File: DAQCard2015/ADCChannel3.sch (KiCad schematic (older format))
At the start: 50 parts, among them U1 LTC6403, U2 AD9219, U3 LTC6403, U4 LTC6403, U5 LTC6403

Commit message: Updates to DAQ Card including FPGA card pinout and completion of ADC Stage
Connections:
- net labels added: 18ana

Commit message: Replaces single ample with 4-channel varients. Greatly reducing part count
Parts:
- removed C1, C11, C15, C16: .01uF, symbol C
- removed C10, C2, C3, C7, C9: .1uF, symbol C
- removed C12, C13, C14, C17, C18, C19, C20, C21, C22, C4, C5, C6: C, symbol C
- removed C8: 2.2uF, symbol CP
- removed R1, R13, R14, R8: Rt, symbol R
- removed R10, R15, R16, R17, R18, R2, R3, R9: Ri, symbol R
- removed R11, R12, R19, R20, R21, R22, R5, R6: Rf, symbol R
- removed R23: 2.7k, symbol R
- removed R24: 1k, symbol R
- removed R7: 10k, symbol R
- removed U1, U3, U4, U5: LTC6403, symbol LTC6403
- removed U2: AD9219, symbol AD9219
- added C32, C33, C34: C, symbol C
- added C35: .01uF, symbol C
- added C36, C37, C38, C40, C41: .1uF, symbol C
- added C39: 2.2uF, symbol CP
- added R25, R26, R27, R28: Rt, symbol R
- added R29: 2.7k, symbol R
- added R30: 1k, symbol R
- added R31: 10k, symbol R
- added RP10: R_PACK8, symbol R_PACK8
- added RP11, RP12: Rf, symbol R_PACK4
- added U8: THS4524IDBTR, symbol THS4524IDBTR
- added U9: AD9219, symbol AD9219
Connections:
- net labels added: 3V3ana, VOCM
- net labels removed: 18ana, 3V3, Vocm
- wire segments 178 -> 192
- no-connect marks 12 -> 4

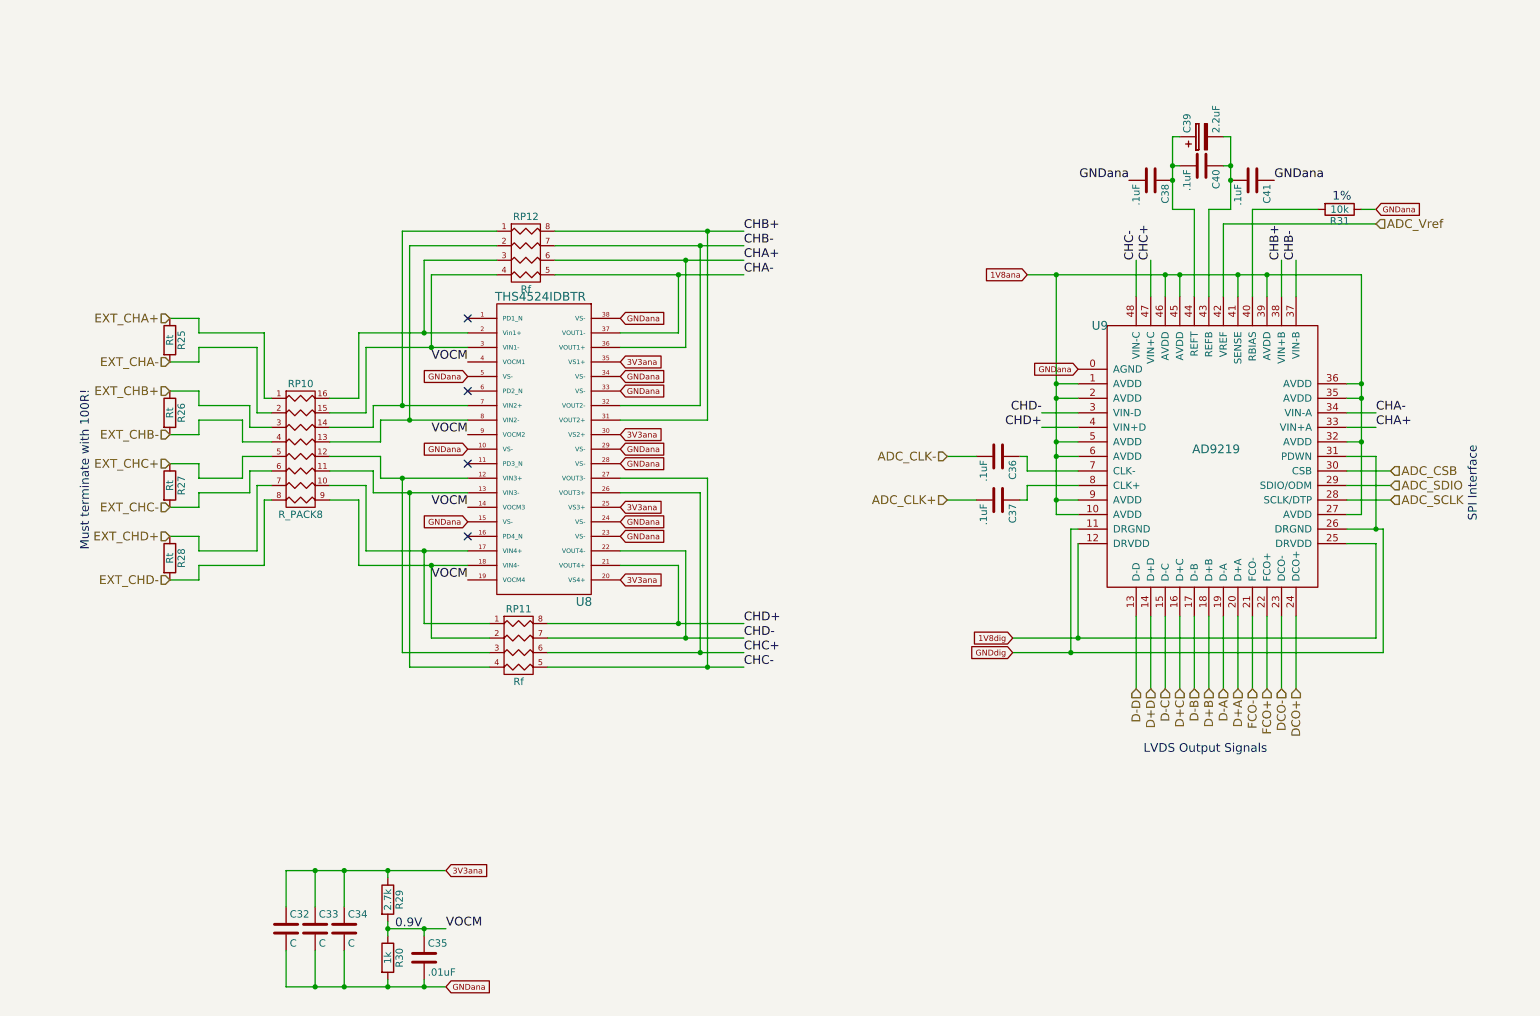
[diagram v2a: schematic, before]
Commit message: Finishes initial version of schematic(mostly). And adds a whole bunch of new footprints!
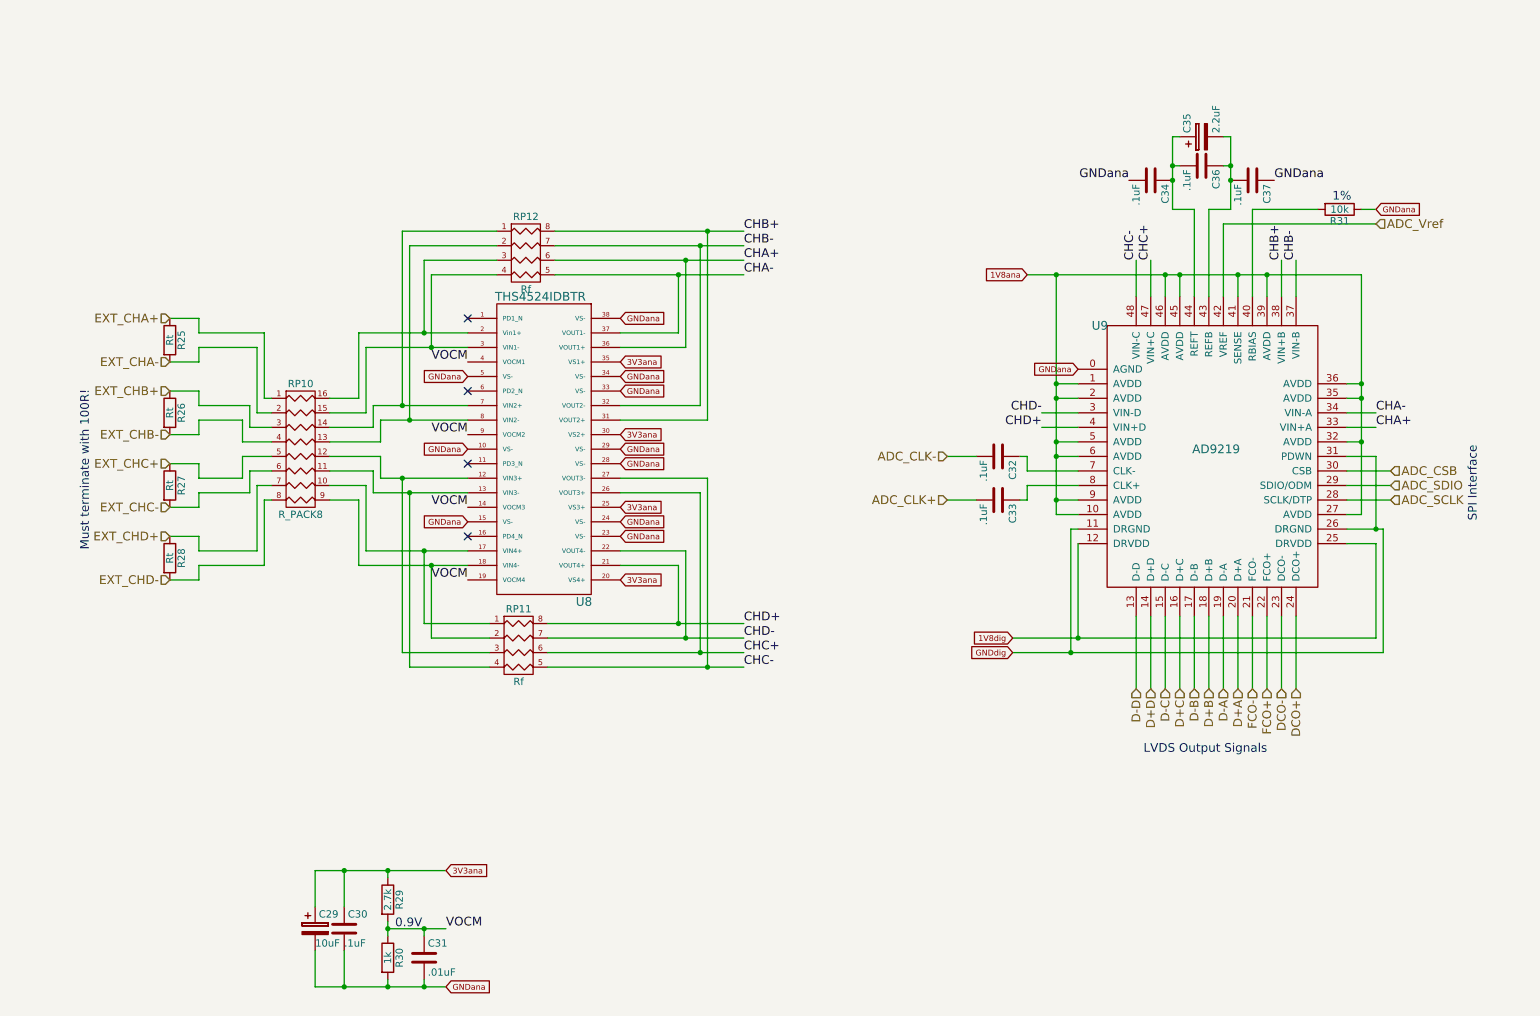
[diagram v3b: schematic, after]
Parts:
- removed C35: .01uF, symbol C
- removed C38, C40, C41: .1uF, symbol C
- removed C39: 2.2uF, symbol CP
- added C29: 10uF, extras:SMD_Cap_3mmDia, symbol CP
- added C30: .1uF, Capacitors_SMD:C_0603, symbol C
- added C31: .01uF, Capacitors_SMD:C_0603, symbol C
- added C35: 2.2uF, extras:SMD_Cap_3mmDia, symbol CP
- C32, C33, C34: value C -> .1uF; footprint (none) -> Capacitors_SMD:C_0603
- C36, C37: footprint (none) -> Capacitors_SMD:C_0603
- R25, R26, R27, R28, R29, R30, R31: footprint (none) -> Resistors_SMD:R_0603
- RP10: footprint (none) -> extras:R8_MNR18
- RP11, RP12: footprint (none) -> extras:R4-MNR04
- U8: footprint (none) -> Housings_SSOP:TSSOP-38_4.4x9.7mm_Pitch0.5mm
- U9: footprint (none) -> SMD_Packages:QFN-48-1EP
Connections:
- net 3V3ana: now also C29.1, C30.1; no longer C32.1, C33.1, C34.1
- net ADC_CLK+: now also C33.2; no longer C37.2
- net ADC_CLK-: now also C32.2; no longer C36.2
- net GNDana: now also C37.1, C29.2, C30.2, C31.2; no longer C32.2, C33.2
- net VOCM: now also C31.1
- net at U9.43 (REFB): now also C36.1, C37.2, C35.2
- net at U9.44 (REFT): now also C34.1, C36.2, C35.1
- net at U9.7 (CLK-): now also C32.1; no longer C36.1
- net at U9.8 (CLK+): now also C33.1; no longer C37.1
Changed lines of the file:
@@
 $Comp
 L AD9219 U9
-U 1 1 55CFF5AE
+U 1 1 55CFF5AD
 P 9050 3700
 F 0 "U9" H 8250 4650 60  0000 C CNN
 F 1 "AD9219" H 9050 3800 60  0000 C CNN
-F 2 "" H 8650 3700 60  0000 C CNN
+F 2 "SMD_Packages:QFN-48-1EP" H 8650 3700 60  0001 C CNN
 F 3 "" H 8650 3700 60  0000 C CNN
 	1    9050 3700
@@
 $Comp
 L R R29
-U 1 1 55CFF5F7
+U 1 1 55CB5787
 P 3350 6700
 F 0 "R29" V 3430 6700 50  0000 C CNN
 F 1 "2.7k" V 3350 6700 50  0000 C CNN
-F 2 "" V 3280 6700 30  0000 C CNN
+F 2 "Resistors_SMD:R_0603" V 3280 6700 30  0001 C CNN
 F 3 "" H 3350 6700 30  0000 C CNN
 	1    3350 6700
@@
 $Comp
 L R R30
-U 1 1 55CFF5E1
+U 1 1 55CB577A
 P 3350 7100
 F 0 "R30" V 3430 7100 50  0000 C CNN
 F 1 "1k" V 3350 7100 50  0000 C CNN
-F 2 "" V 3280 7100 30  0000 C CNN
+F 2 "Resistors_SMD:R_0603" V 3280 7100 30  0001 C CNN
 F 3 "" H 3350 7100 30  0000 C CNN
 	1    3350 7100
@@
 Must terminate with 100R!
 $Comp
-L C C32
-U 1 1 55CFF5C8
-P 2650 6900
-F 0 "C32" H 2675 7000 50  0000 L CNN
-F 1 "C" H 2675 6800 50  0000 L CNN
-F 2 "" H 2688 6750 30  0000 C CNN
-F 3 "" H 2650 6900 60  0000 C CNN
-	1    2650 6900
-	1    0    0    -1
-$EndComp
-$Comp
-L C C33
-U 1 1 55CFF5B8
-P 2850 6900
-F 0 "C33" H 2875 7000 50  0000 L CNN
-F 1 "C" H 2875 6800 50  0000 L CNN
-F 2 "" H 2888 6750 30  0000 C CNN
-F 3 "" H 2850 6900 60  0000 C CNN
-	1    2850 6900
-	1    0    0    -1
-$EndComp
-$Comp
-L C C34
-U 1 1 55CFF5BE
+L C C30
+U 1 1 55CB575B
 P 3050 6900
-F 0 "C34" H 3075 7000 50  0000 L CNN
-F 1 "C" H 3075 6800 50  0000 L CNN
-F 2 "" H 3088 6750 30  0000 C CNN
+F 0 "C30" H 3075 7000 50  0000 L CNN
+F 1 ".1uF" H 3050 6800 50  0000 L CNN
+F 2 "Capacitors_SMD:C_0603" H 3088 6750 30  0001 C CNN
 F 3 "" H 3050 6900 60  0000 C CNN
 	1    3050 6900
@@
 ADC_SCLK
 $Comp
-L C C36
-U 1 1 55CFF5C1
+L C C32
+U 1 1 55CB5767
 P 7550 3650
-F 0 "C36" H 7575 3750 50  0000 L CNN
+F 0 "C32" H 7575 3750 50  0000 L CNN
 F 1 ".1uF" H 7575 3550 50  0000 L CNN
-F 2 "" H 7588 3500 30  0000 C CNN
+F 2 "Capacitors_SMD:C_0603" H 7588 3500 30  0001 C CNN
 F 3 "" H 7550 3650 60  0000 C CNN
 	1    7550 3650
@@
 $EndComp
 $Comp
-L C C37
-U 1 1 55CFF5E3
+L C C33
+U 1 1 55CB574B
 P 7550 3950
-F 0 "C37" H 7575 4050 50  0000 L CNN
+F 0 "C33" H 7575 4050 50  0000 L CNN
 F 1 ".1uF" H 7575 3850 50  0000 L CNN
-F 2 "" H 7588 3800 30  0000 C CNN
+F 2 "Capacitors_SMD:C_0603" H 7588 3800 30  0001 C CNN
 F 3 "" H 7550 3950 60  0000 C CNN
 	1    7550 3950
@@
 DCO+
 $Comp
-L C C41
-U 1 1 55CFF5FB
+L C C37
+U 1 1 55CB5791
 P 9300 1750
-F 0 "C41" H 9325 1850 50  0000 L CNN
+F 0 "C37" H 9325 1850 50  0000 L CNN
 F 1 ".1uF" H 9325 1650 50  0000 L CNN
-F 2 "" H 9338 1600 30  0000 C CNN
+F 2 "Capacitors_SMD:C_0603" H 9338 1600 30  0001 C CNN
 F 3 "" H 9300 1750 60  0000 C CNN
 	1    9300 1750
@@
 $EndComp
 $Comp
-L C C38
-U 1 1 55CFF5D4
+L C C34
+U 1 1 55CB576A
 P 8600 1750
-F 0 "C38" H 8625 1850 50  0000 L CNN
+F 0 "C34" H 8625 1850 50  0000 L CNN
 F 1 ".1uF" H 8625 1650 50  0000 L CNN
-F 2 "" H 8638 1600 30  0000 C CNN
+F 2 "Capacitors_SMD:C_0603" H 8638 1600 30  0001 C CNN
 F 3 "" H 8600 1750 60  0000 C CNN
 	1    8600 1750
@@
 $EndComp
 $Comp
-L C C40
-U 1 1 55CFF5D8
+L C C36
+U 1 1 55CFF5D5
 P 8950 1650
-F 0 "C40" H 8975 1750 50  0000 L CNN
+F 0 "C36" H 8975 1750 50  0000 L CNN
 F 1 ".1uF" H 8975 1550 50  0000 L CNN
-F 2 "" H 8988 1500 30  0000 C CNN
+F 2 "Capacitors_SMD:C_0603" H 8988 1500 30  0001 C CNN
 F 3 "" H 8950 1650 60  0000 C CNN
 	1    8950 1650
@@
 GNDana
 $Comp
-L CP C39
-U 1 1 55CFF605
+L CP C35
+U 1 1 55CB5797
 P 8950 1450
-F 0 "C39" H 8975 1550 50  0000 L CNN
+F 0 "C35" H 8975 1550 50  0000 L CNN
 F 1 "2.2uF" H 8975 1350 50  0000 L CNN
-F 2 "" H 8988 1300 30  0000 C CNN
+F 2 "extras:SMD_Cap_3mmDia" H 8988 1300 30  0001 C CNN
 F 3 "" H 8950 1450 60  0000 C CNN
 	1    8950 1450
@@
 $Comp
 L R R31
-U 1 1 55CFF5EE
+U 1 1 55CB5783
 P 9900 1950
 F 0 "R31" V 9980 1950 50  0000 C CNN
 F 1 "10k" V 9900 1950 50  0000 C CNN
-F 2 "" V 9830 1950 30  0000 C CNN
+F 2 "Resistors_SMD:R_0603" V 9830 1950 30  0001 C CNN
 F 3 "" H 9900 1950 30  0000 C CNN
 	1    9900 1950
@@
 $Comp
 L THS4524IDBTR U8
-U 1 1 55CFF609
+U 1 1 55CB579A
 P 4400 3700
 F 0 "U8" H 4700 2750 60  0000 C CNN
 F 1 "THS4524IDBTR" H 4400 4850 60  0000 C CNN
-F 2 "" H 4600 3800 60  0000 C CNN
+F 2 "Housings_SSOP:TSSOP-38_4.4x9.7mm_Pitch0.5mm" H 4600 3800 60  0001 C CNN
 F 3 "" H 4600 3800 60  0000 C CNN
 	1    4400 3700
@@
 $EndComp
 $Comp
-L C C35
-U 1 1 55CFF60F
+L C C31
+U 1 1 55CB57A1
 P 3600 7100
-F 0 "C35" H 3625 7200 50  0000 L CNN
+F 0 "C31" H 3625 7200 50  0000 L CNN
 F 1 ".01uF" H 3625 7000 50  0000 L CNN
-F 2 "" H 3638 6950 30  0000 C CNN
+F 2 "Capacitors_SMD:C_0603" H 3638 6950 30  0001 C CNN
 F 3 "" H 3600 7100 60  0000 C CNN
 	1    3600 7100
@@
 Connection ~ 3600 6900
 Wire Wire Line
-	2650 6500 3750 6500
-Wire Wire Line
 	3050 6500 3050 6750
 Connection ~ 3350 6500
@@
 Connection ~ 3050 6500
 Wire Wire Line
-	2650 6500 2650 6750
-Connection ~ 2850 6500
-Wire Wire Line
-	2650 7300 3750 7300
-Wire Wire Line
 	3050 7300 3050 7050
 Wire Wire Line
 	2850 7300 2850 7050
 Connection ~ 3050 7300
-Wire Wire Line
-	2650 7300 2650 7050
-Connection ~ 2850 7300
 Wire Wire Line
 	3600 7300 3600 7250
@@
 $Comp
 L R R28
-U 1 1 55CFF615
+U 1 1 55CB57A7
 P 1850 4350
 F 0 "R28" V 1930 4350 50  0000 C CNN
 F 1 "Rt" V 1850 4350 50  0000 C CNN
-F 2 "" V 1780 4350 30  0000 C CNN
+F 2 "Resistors_SMD:R_0603" V 1780 4350 30  0001 C CNN
 F 3 "" H 1850 4350 30  0000 C CNN
 	1    1850 4350
@@
 $Comp
 L R R27
-U 1 1 55CFF61F
+U 1 1 55CB57AF
 P 1850 3850
 F 0 "R27" V 1930 3850 50  0000 C CNN
 F 1 "Rt" V 1850 3850 50  0000 C CNN
-F 2 "" V 1780 3850 30  0000 C CNN
+F 2 "Resistors_SMD:R_0603" V 1780 3850 30  0001 C CNN
 F 3 "" H 1850 3850 30  0000 C CNN
 	1    1850 3850
@@
 $Comp
 L R R26
-U 1 1 55CFF626
+U 1 1 55CB57B7
 P 1850 3350
 F 0 "R26" V 1930 3350 50  0000 C CNN
 F 1 "Rt" V 1850 3350 50  0000 C CNN
-F 2 "" V 1780 3350 30  0000 C CNN
+F 2 "Resistors_SMD:R_0603" V 1780 3350 30  0001 C CNN
 F 3 "" H 1850 3350 30  0000 C CNN
 	1    1850 3350
@@
 $Comp
 L R R25
-U 1 1 55CFF62C
+U 1 1 55CB57BF
 P 1850 2850
 F 0 "R25" V 1930 2850 50  0000 C CNN
 F 1 "Rt" V 1850 2850 50  0000 C CNN
-F 2 "" V 1780 2850 30  0000 C CNN
+F 2 "Resistors_SMD:R_0603" V 1780 2850 30  0001 C CNN
 F 3 "" H 1850 2850 30  0000 C CNN
 	1    1850 2850
@@
 $Comp
 L R_PACK4 RP11
-U 1 1 55CFF635
+U 1 1 55CB57C6
 P 4250 5150
 F 0 "RP11" H 4250 5600 50  0000 C CNN
 F 1 "Rf" H 4250 5100 50  0000 C CNN
-F 2 "" H 4250 5150 60  0000 C CNN
+F 2 "extras:R4-MNR04" H 4250 5150 60  0001 C CNN
 F 3 "" H 4250 5150 60  0000 C CNN
 	1    4250 5150
@@
 $Comp
 L R_PACK4 RP12
-U 1 1 55CFF63D
+U 1 1 55CB5752
 P 4300 2450
 F 0 "RP12" H 4300 2900 50  0000 C CNN
 F 1 "Rf" H 4300 2400 50  0000 C CNN
-F 2 "" H 4300 2450 60  0000 C CNN
+F 2 "extras:R4-MNR04" H 4300 2450 60  0001 C CNN
 F 3 "" H 4300 2450 60  0000 C CNN
 	1    4300 2450
@@
 $Comp
 L R_PACK8 RP10
-U 1 1 55CFF640
+U 1 1 55CB57CD
 P 2750 3600
 F 0 "RP10" H 2750 4050 50  0000 C CNN
 F 1 "R_PACK8" H 2750 3150 50  0000 C CNN
-F 2 "" H 2750 3600 60  0000 C CNN
+F 2 "extras:R8_MNR18" H 2750 3600 60  0001 C CNN
 F 3 "" H 2750 3600 60  0000 C CNN
 	1    2750 3600
@@
 Text GLabel 10150 1950 2    40   Input ~ 0
 GNDana
+Wire Wire Line
+	3750 6500 2850 6500
+Wire Wire Line
+	2850 7300 3750 7300
+$Comp
+L CP C29
+U 1 1 55CB573F
+P 2850 6900
+F 0 "C29" H 2875 7000 50  0000 L CNN
+F 1 "10uF" H 2850 6800 50  0000 L CNN
+F 2 "extras:SMD_Cap_3mmDia" H 2888 6750 30  0001 C CNN
+F 3 "" H 2850 6900 60  0000 C CNN
+	1    2850 6900
+	1    0    0    -1
+$EndComp
 $EndSCHEMATC

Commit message: Adds a more-or-less complete BOM to DAQ Card
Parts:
- C31: value .01uF -> 10000pF
- RP10: value R_PACK8 -> Ri
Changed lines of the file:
@@
 $Descr A4 11693 8268
 encoding utf-8
-Sheet 3 13
+Sheet 6 13
 Title ""
 Date ""
@@
 P 3600 7100
 F 0 "C31" H 3625 7200 50  0000 L CNN
-F 1 ".01uF" H 3625 7000 50  0000 L CNN
+F 1 "10000pF" H 3625 7000 50  0000 L CNN
 F 2 "Capacitors_SMD:C_0603" H 3638 6950 30  0001 C CNN
 F 3 "" H 3600 7100 60  0000 C CNN
@@
 P 2750 3600
 F 0 "RP10" H 2750 4050 50  0000 C CNN
-F 1 "R_PACK8" H 2750 3150 50  0000 C CNN
+F 1 "Ri" H 2750 3150 50  0000 C CNN
 F 2 "extras:R8_MNR18" H 2750 3600 60  0001 C CNN
 F 3 "" H 2750 3600 60  0000 C CNN

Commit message: Updates to DAQCard2015, especially to power systems
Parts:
- C29, C35: footprint extras:SMD_Cap_3mmDia -> Capacitors_SMD:C_0805
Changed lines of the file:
@@
 F 0 "C35" H 8975 1550 50  0000 L CNN
 F 1 "2.2uF" H 8975 1350 50  0000 L CNN
-F 2 "extras:SMD_Cap_3mmDia" H 8988 1300 30  0001 C CNN
+F 2 "Capacitors_SMD:C_0805" H 8988 1300 30  0001 C CNN
 F 3 "" H 8950 1450 60  0000 C CNN
 	1    8950 1450
@@
 F 0 "C29" H 2875 7000 50  0000 L CNN
 F 1 "10uF" H 2850 6800 50  0000 L CNN
-F 2 "extras:SMD_Cap_3mmDia" H 2888 6750 30  0001 C CNN
+F 2 "Capacitors_SMD:C_0805" H 2888 6750 30  0001 C CNN
 F 3 "" H 2850 6900 60  0000 C CNN
 	1    2850 6900
